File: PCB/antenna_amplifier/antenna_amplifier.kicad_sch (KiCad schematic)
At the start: 0 parts

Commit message: Populate antenna_amplifier schematic with full signal chain
Place all ICs (LMP7721, LMP7715, PCM1808, CS8406, 2x ADM7150),
passive components (R1/R3 220k filter, R2 1k + C3 4.7u feedback,
R4 470R guard drive), connectors (ANT_IN, SPDIF_OUT, PWR_IN),
and power symbols (+9V, +5VA, +3V3D, GND).

Wire signal path: antenna → RC filter → LMP7721 preamp with
frequency-dependent feedback → PCM1808 ADC (I2S) → CS8406
SPDIF TX → output connector. Guard driver (LMP7715 unity-gain)
drives PCB guard ring. Dual ADM7150 LDOs for analog/digital
supply rails.

All CS8406 config pins tied for HW mode, I2S input, 256fs.
Netlist verified correct (28 nets, 0 unconnected pins).
Remaining ERC: lib_symbol_mismatch (cosmetic), label placement,
PWR_FLAG needed on GND/+9V — all fixable in KiCad editor.

Co-Authored-By: Claude Opus 4.6 <noreply@anthropic.com>
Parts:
- added C3: 4.7u, symbol Device:C
- added J1: ANT_IN, symbol Connector:Conn_01x02_Pin
- added J2: SPDIF_OUT, symbol Connector:Conn_01x02_Pin
- added J3: PWR_IN, symbol Connector:Conn_01x02_Pin
- added R1, R3: 220k, symbol Device:R
- added R2: 1k, symbol Device:R
- added R4: 470, symbol Device:R
- added U1: LMP7721, Package_SO:SOIC-8_3.9x4.9mm_P1.27mm, symbol antenna_amplifier:LMP7721
- added U2: LMP7715, Package_TO_SOT_SMD:SOT-23-5, symbol antenna_amplifier:LMP7715
- added U3: PCM1808, Package_SO:TSSOP-14_4.4x5mm_P0.65mm, symbol antenna_amplifier:PCM1808
- added U4: CS8406, Package_SO:TSSOP-28_4.4x9.7mm_P0.65mm, symbol antenna_amplifier:CS8406
- added U5: ADM7150-5.0, Package_SO:SOIC-8-1EP_3.9x4.9mm_P1.27mm_EP2.41x3.1mm, symbol antenna_amplifier:ADM7150
- added U6: ADM7150-3.3, Package_SO:SOIC-8-1EP_3.9x4.9mm_P1.27mm_EP2.41x3.1mm, symbol antenna_amplifier:ADM7150
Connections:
- new net: R1.2, R3.1
- new net: R4.1, U2.1 (OUT), U2.4 (-IN)
- new net +3V3D: U3.4 (VDD), U4.16 (CEN), U4.23 (VL), U4.5 (SFMT1), U4.6 (VD), U4.9 (~{RST}), U6.2 (VOUT)
- new net +5VA: U1.8 (V+), U2.5 (V+), U3.3 (VCC), U5.2 (VOUT)
- new net +9V: J3.1 (Pin_1), U5.7 (EN), U5.8 (VIN), U6.7 (EN), U6.8 (VIN)
- new net ANT_IN: J1.1 (Pin_1), R1.1
- new net BCK: U3.8 (BCK), U4.13 (ISCLK)
- new net BIAS_MID: U3.1 (VREF), U3.14 (VINR)
- new net BYP_A: U5.3 (BYP)
- new net BYP_D: U6.3 (BYP)
- new net DOUT: U3.9 (DOUT), U4.14 (SDIN)
- new net FILT_OUT: R3.2, U1.1 (IN+), U2.3 (+IN)
- new net GND: J1.2 (Pin_2), J3.2 (Pin_2), U1.4 (V-), U2.2 (V-), U3.10 (MD0), U3.11 (MD1), U3.12 (FMT), U3.2 (AGND), U3.5 (DGND), U4.1 (COPY/C), U4.10 (APMS), U4.11 (TCBLD), U4.17 (V), U4.18 (U), U4.19 (AUDIO), U4.2 (TEST), U4.20 (HWCK0), U4.22 (GND), U4.24 (~{H/S}), U4.27 (HWCK1), U4.28 (ORIG), U4.3 (EMPH), U4.4 (SFMT0), U4.7 (TEST), U4.8 (TEST), U5.4 (GND), U5.9 (EPAD), U6.4 (GND), U6.9 (EPAD)
- new net GUARD_RING: R4.2, U1.2 (GRD), U1.7 (GRD)
- new net LRCK: U3.7 (LRCK), U4.12 (ILRCK)
- new net MCLK: U3.6 (SCKI), U4.21 (OMCK)
- new net PREAMP_OUT: C3.1, C3.2, R2.1, R2.2, U1.3 (IN-), U1.6 (VOUT), U3.13 (VINL)
- new net REFS_A: U5.5 (REF_SENSE)
- new net REFS_D: U6.5 (REF_SENSE)
- new net REF_A: U5.6 (REF)
- new net REF_D: U6.6 (REF)
- new net SPDIF_N: J2.2 (Pin_2), U4.25 (TXN)
- new net SPDIF_P: J2.1 (Pin_1), U4.26 (TXP)
- new net TCBL: U4.15 (TCBL)
- new net VREG_A: U5.1 (VREG)
- new net VREG_D: U6.1 (VREG)
- no-connect marks 0 -> 1
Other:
- title: (none) -> ELARA  ELF/VLF Atmospheric Radio Analyser

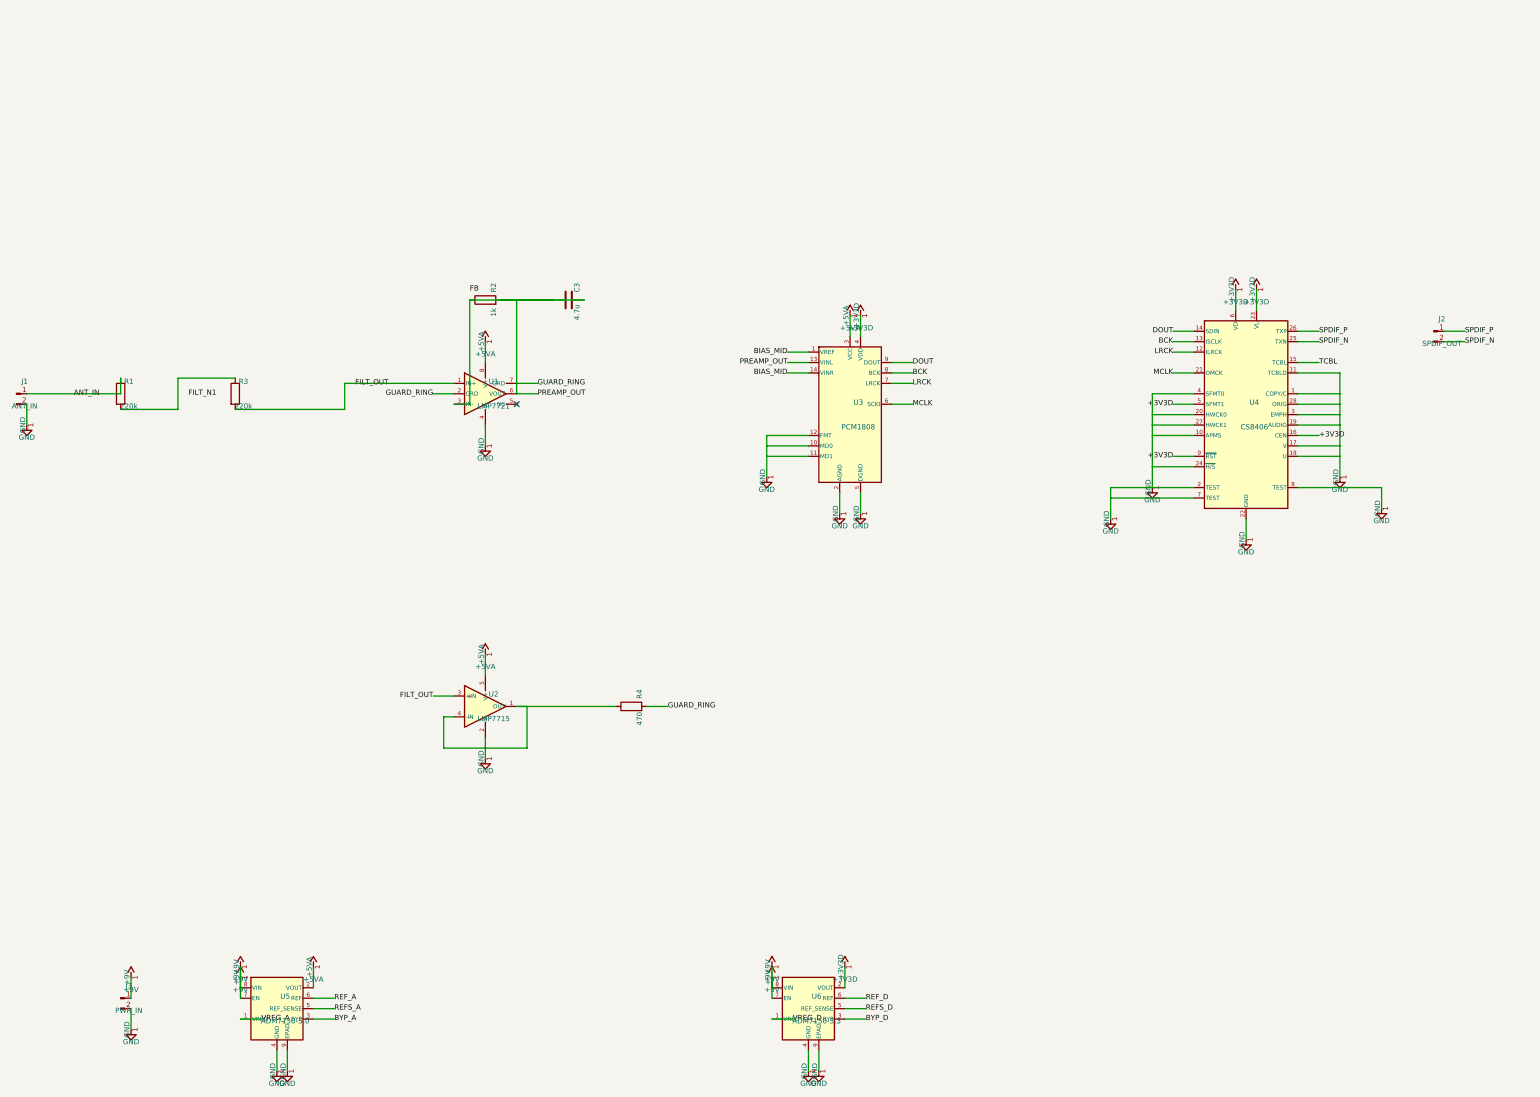
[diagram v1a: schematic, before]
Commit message: Fix preamp feedback, add bias/oscillator/AA filter (Phases 1-4)
Phase 1 — Fix feedback network for 20 dB ELF gain:
  R2→Rf (9.1k), C3→Cf (150nF) in parallel IN-→VOUT,
  add Rg (1k) from IN-→BIAS_MID. G=10.1 (20dB) flat across
  ELF, rolls off above 117 Hz. Correct single-supply biasing
  via 2.5V BIAS_MID reference.

Phase 2 — Add antenna bias circuit (§3.7):
  U7 LMP7715 unity-gain follower, R5/R6 47k matched divider
  (+5VA→GND → 2.5V), C7 4700µF bypass, C8 100nF supply bypass,
  J4 jumper header for physical antenna connection.
  BIAS_MID net shared with preamp Rg reference.

Phase 3 — Add 24.576 MHz MEMS oscillator:
  Y1 MEMS_OSC with R_S 33R series resistor, C9 100nF bypass.
  MCLK net drives PCM1808 SCKI and CS8406 OMCK.
  New MEMS_OSC symbol added to project library.

Phase 4 — Add anti-aliasing filter (§3.4):
  R_AA (10k) + C_AA (100nF) passive RC, fc=159 Hz.
  Inserted between PREAMP_OUT and AA_OUT→PCM1808 VINL.
  Combined with preamp rolloff (117 Hz) gives ~2nd-order
  filtering for ELF-focused design.

Co-Authored-By: Claude Opus 4.6 (1M context) <noreply@anthropic.com>
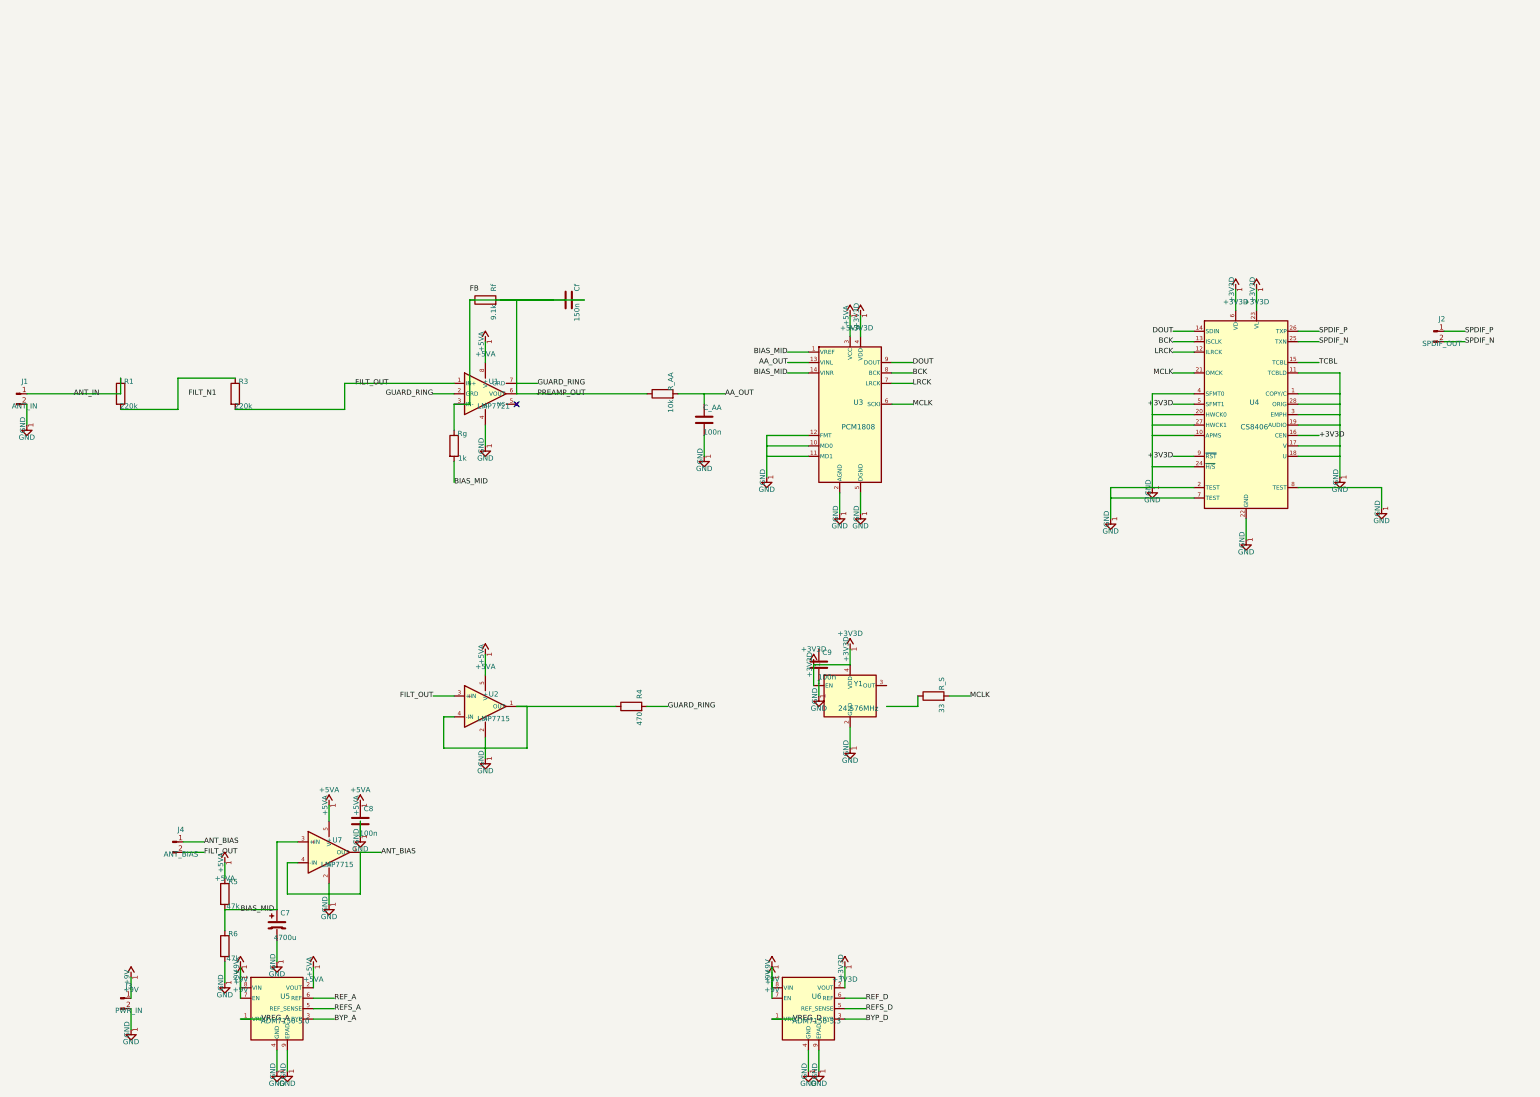
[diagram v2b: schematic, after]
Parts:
- added C7: 4700u, symbol Device:C_Polarized
- added C8, C9, C_AA: 100n, symbol Device:C
- added J4: ANT_BIAS, symbol Connector:Conn_01x02_Pin
- added R5, R6: 47k, symbol Device:R
- added R_AA: 10k, symbol Device:R
- added R_S: 33, symbol Device:R
- added Rg: 1k, symbol Device:R
- added U7: LMP7715, Package_TO_SOT_SMD:SOT-23-5, symbol antenna_amplifier:LMP7715
- added Y1: 24.576MHz, Package_TO_SOT_SMD:SOT-23-5, symbol antenna_amplifier:MEMS_OSC
- Cf: renamed from C3; value 4.7u -> 150n
- Rf: renamed from R2; value 1k -> 9.1k
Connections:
- net +3V3D: now also Y1.1 (EN), Y1.4 (VDD)
- net +5VA: now also C8.1, R5.1, U7.5 (V+)
- net BIAS_MID: now also C7.1, R5.2, R6.1, Rg.2, U7.3 (+IN)
- net FILT_OUT: now also J4.2 (Pin_2)
- net GND: now also C7.2, C8.2, C9.2, C_AA.2, R6.2, U7.2 (V-), Y1.2 (GND)
- net MCLK: now also R_S.2
- net PREAMP_OUT: now also R_AA.1, Rg.1; no longer U3.13 (VINL)
- new net AA_OUT: C_AA.1, R_AA.2, U3.13 (VINL)
- new net ANT_BIAS: J4.1 (Pin_1), U7.1 (OUT), U7.4 (-IN)
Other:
- title: ELARA  ELF/VLF Atmospheric Radio Analyser -> ELARA � ELF/VLF Atmospheric Radio Analyser

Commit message: Add transformers, fix config pins, update PLAN.md (Phases 5-8)
Phase 5 — Add audio transformers + dual output:
  TR1 (S22082) for S/PDIF coax → J2 RCA,
  TR2 (S22083) for AES/EBU balanced → J5 connector.
  Coupling caps C_T1/C_T2 (100nF) on primaries.
  Both driven from CS8406 TXP/TXN simultaneously.
  New XFMR_Audio symbol added to project library.

Phase 6 — Fix PCM1808 config for 96 kSPS default:
  MD1 changed from GND to +5VA (MD1=H, MD0=L → 256×fs).

Phase 8 — Update PLAN.md:
  - Revised §3.1: new feedback topology (Rf=9.1k, Cf=150nF,
    Rg=1k to BIAS_MID), 20 dB flat ELF gain, 117 Hz rolloff
  - Documented ELF-only design decision (VLF dropped)
  - Updated §3.4: simplified AA filter (R_AA 10k + C_AA 100nF,
    fc=159 Hz, combined with preamp rolloff for 2nd-order)
  - Title updated: ELF/VLF → ELF

Phase 7 (bypass caps) deferred to KiCad GUI placement.

Co-Authored-By: Claude Opus 4.6 (1M context) <noreply@anthropic.com>
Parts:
- added C_T1, C_T2: 100n, symbol Device:C
- added J5: AES_EBU, symbol Connector:Conn_01x02_Pin
- added TR1: S22082, symbol antenna_amplifier:XFMR_Audio
- added TR2: S22083, symbol antenna_amplifier:XFMR_Audio
- J2: value SPDIF_OUT -> SPDIF_COAX
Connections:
- net GND is gone; now on net +5VA: C7.2, C8.2, C9.2, C_AA.2, J1.2 (Pin_2), J3.2 (Pin_2), R6.2, U1.4 (V-), U2.2 (V-), U3.10 (MD0), U3.11 (MD1), U3.12 (FMT), U3.2 (AGND), U3.5 (DGND), U4.1 (COPY/C), U4.10 (APMS), U4.11 (TCBLD), U4.17 (V), U4.18 (U), U4.19 (AUDIO), U4.2 (TEST), U4.20 (HWCK0), U4.22 (GND), U4.24 (~{H/S}), U4.27 (HWCK1), U4.28 (ORIG), U4.3 (EMPH), U4.4 (SFMT0), U4.7 (TEST), U4.8 (TEST), U5.4 (GND), U5.9 (EPAD), U6.4 (GND), U6.9 (EPAD), U7.2 (V-), Y1.2 (GND)
- net +5VA: now also U4.26 (TXP), C_T1.1, C_T2.1
- net SPDIF_N: now also TR1.2 (P2), TR2.2 (P2); no longer J2.2 (Pin_2)
- net SPDIF_P: no longer names the net of J2.1 (Pin_1)
- net SPDIF_P: now also TR1.3 (S1); no longer U4.26 (TXP)
- new net: C_T1.2, TR1.1 (P1)
- new net: C_T2.2, TR2.1 (P1)
- new net: J5.1 (Pin_1), TR2.3 (S1)
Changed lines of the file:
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@@
 	)
+	(symbol
+		(lib_id "antenna_amplifier:XFMR_Audio")
+		(at 368.3 55.88 0)
+		(unit 1)
+		(exclude_from_sim no) (in_bom yes) (on_board yes) (dnp no)
+		(property "Reference" "TR1" (at 368.3 46.99 0) (effects (font (size 1.27 1.27))))
+		(property "Value" "S22082" (at 368.3 64.77 0) (effects (font (size 1.27 1.27))))
+		(property "Datasheet" "~" (at 368.3 55.88 0) (effects (font (size 1.27 1.27)) (hide yes)))
+		(instances (project "antenna_amplifier"
+			(path "/09f45598-3e76-49a4-ba12-a3a92a2874f1" (reference "TR1") (unit 1)))))
+	(symbol
+		(lib_id "antenna_amplifier:XFMR_Audio")
+		(at 368.3 78.74 0)
+		(unit 1)
+		(exclude_from_sim no) (in_bom yes) (on_board yes) (dnp no)
+		(property "Reference" "TR2" (at 368.3 69.85 0) (effects (font (size 1.27 1.27))))
+		(property "Value" "S22083" (at 368.3 87.63 0) (effects (font (size 1.27 1.27))))
+		(property "Datasheet" "~" (at 368.3 78.74 0) (effects (font (size 1.27 1.27)) (hide yes)))
+		(instances (project "antenna_amplifier"
+			(path "/09f45598-3e76-49a4-ba12-a3a92a2874f1" (reference "TR2") (unit 1)))))
 	(symbol
 		(lib_id "Connector:Conn_01x02_Pin")
-		(at 370.84 63.5 0)
-		(unit 1)
-		(exclude_from_sim no)
-		(in_bom yes)
-		(on_board yes)
-		(dnp no)
-		(property "Reference" "J2"
-			(at 372.84 60.5 0)
-			(effects
-				(font
-					(size 1.27 1.27)
-				)
-			)
-		)
-		(property "Value" "SPDIF_OUT"
-			(at 372.84 66.5 0)
-			(effects
-				(font
-					(size 1.27 1.27)
-				)
-			)
-		)
-		(property "Datasheet" "~"
-			(at 370.84 63.5 0)
-			(effects
-				(font
-					(size 1.27 1.27)
-				)
-				(hide yes)
-			)
-		)
-		(instances
-			(project "antenna_amplifier"
-				(path "/09f45598-3e76-49a4-ba12-a3a92a2874f1"
-					(reference "J2")
-					(unit 1)
-				)
-			)
-		)
-	)
+		(at 386.08 55.88 0)
+		(unit 1)
+		(exclude_from_sim no) (in_bom yes) (on_board yes) (dnp no)
+		(property "Reference" "J2" (at 388.08 52.88 0) (effects (font (size 1.27 1.27))))
+		(property "Value" "SPDIF_COAX" (at 388.08 58.88 0) (effects (font (size 1.27 1.27))))
+		(property "Datasheet" "~" (at 386.08 55.88 0) (effects (font (size 1.27 1.27)) (hide yes)))
+		(instances (project "antenna_amplifier"
+			(path "/09f45598-3e76-49a4-ba12-a3a92a2874f1" (reference "J2") (unit 1)))))
+	(symbol
+		(lib_id "Connector:Conn_01x02_Pin")
+		(at 386.08 78.74 0)
+		(unit 1)
+		(exclude_from_sim no) (in_bom yes) (on_board yes) (dnp no)
+		(property "Reference" "J5" (at 388.08 75.74 0) (effects (font (size 1.27 1.27))))
+		(property "Value" "AES_EBU" (at 388.08 81.74 0) (effects (font (size 1.27 1.27))))
+		(property "Datasheet" "~" (at 386.08 78.74 0) (effects (font (size 1.27 1.27)) (hide yes)))
+		(instances (project "antenna_amplifier"
+			(path "/09f45598-3e76-49a4-ba12-a3a92a2874f1" (reference "J5") (unit 1)))))
+	(symbol
+		(lib_id "Device:C")
+		(at 355.6 50.8 90)
+		(unit 1)
+		(exclude_from_sim no) (in_bom yes) (on_board yes) (dnp no)
+		(property "Reference" "C_T1" (at 355.6 47.8 0) (effects (font (size 1.27 1.27))))
+		(property "Value" "100n" (at 355.6 53.8 0) (effects (font (size 1.27 1.27))))
+		(property "Datasheet" "~" (at 355.6 50.8 0) (effects (font (size 1.27 1.27)) (hide yes)))
+		(instances (project "antenna_amplifier"
+			(path "/09f45598-3e76-49a4-ba12-a3a92a2874f1" (reference "C_T1") (unit 1)))))
+	(symbol
+		(lib_id "Device:C")
+		(at 355.6 73.66 90)
+		(unit 1)
+		(exclude_from_sim no) (in_bom yes) (on_board yes) (dnp no)
+		(property "Reference" "C_T2" (at 355.6 70.66 0) (effects (font (size 1.27 1.27))))
+		(property "Value" "100n" (at 355.6 76.66 0) (effects (font (size 1.27 1.27))))
+		(property "Datasheet" "~" (at 355.6 73.66 0) (effects (font (size 1.27 1.27)) (hide yes)))
+		(instances (project "antenna_amplifier"
+			(path "/09f45598-3e76-49a4-ba12-a3a92a2874f1" (reference "C_T2") (unit 1)))))
+	(wire (pts (xy 351.79 50.8) (xy 347.98 50.8))
+		(stroke (width 0) (type solid)))
+	(label "SPDIF_P" (at 347.98 50.8 180)
+		(effects (font (size 1.27 1.27))))
+	(wire (pts (xy 359.41 50.8) (xy 363.22 50.8))
+		(stroke (width 0) (type solid)))
+	(wire (pts (xy 363.22 60.96) (xy 358.14 60.96))
+		(stroke (width 0) (type solid)))
+	(label "SPDIF_N" (at 358.14 60.96 180)
+		(effects (font (size 1.27 1.27))))
+	(wire (pts (xy 373.38 50.8) (xy 378.46 50.8))
+		(stroke (width 0) (type solid)))
+	(wire (pts (xy 378.46 50.8) (xy 378.46 55.88))
+		(stroke (width 0) (type solid)))
+	(wire (pts (xy 378.46 55.88) (xy 388.62 55.88))
+		(stroke (width 0) (type solid)))
+	(wire (pts (xy 373.38 60.96) (xy 381 60.96))
+		(stroke (width 0) (type solid)))
+	(wire (pts (xy 381 60.96) (xy 381 53.34))
+		(stroke (width 0) (type solid)))
+	(wire (pts (xy 381 53.34) (xy 388.62 53.34))
+		(stroke (width 0) (type solid)))
+	(wire (pts (xy 351.79 73.66) (xy 347.98 73.66))
+		(stroke (width 0) (type solid)))
+	(label "SPDIF_P" (at 347.98 73.66 180)
+		(effects (font (size 1.27 1.27))))
+	(wire (pts (xy 359.41 73.66) (xy 363.22 73.66))
+		(stroke (width 0) (type solid)))
+	(wire (pts (xy 363.22 83.82) (xy 358.14 83.82))
+		(stroke (width 0) (type solid)))
+	(label "SPDIF_N" (at 358.14 83.82 180)
+		(effects (font (size 1.27 1.27))))
+	(wire (pts (xy 373.38 73.66) (xy 378.46 73.66))
+		(stroke (width 0) (type solid)))
+	(wire (pts (xy 378.46 73.66) (xy 378.46 78.74))
+		(stroke (width 0) (type solid)))
+	(wire (pts (xy 378.46 78.74) (xy 388.62 78.74))
+		(stroke (width 0) (type solid)))
+	(wire (pts (xy 373.38 83.82) (xy 381 83.82))
+		(stroke (width 0) (type solid)))
+	(wire (pts (xy 381 83.82) (xy 381 76.2))
+		(stroke (width 0) (type solid)))
+	(wire (pts (xy 381 76.2) (xy 388.62 76.2))
+		(stroke (width 0) (type solid)))
 	(symbol
 		(lib_id "Connector:Conn_01x02_Pin")
@@
 	(wire
 		(pts
-			(xy 218.44 93.98) (xy 208.28 93.98)
-		)
-		(stroke
-			(width 0)
-			(type solid)
-		)
-	)
+			(xy 218.44 93.98) (xy 218.44 88.9)
+		)
+		(stroke
+			(width 0)
+			(type solid)
+		)
+	)
+	(symbol
+		(lib_id "power:+5VA")
+		(at 218.44 88.9 0)
+		(unit 1)
+		(exclude_from_sim no) (in_bom yes) (on_board yes) (dnp no)
+		(property "Reference" "#PWR80" (at 218.44 86.9 0) (effects (font (size 1.27 1.27)) (hide yes)))
+		(property "Value" "+5VA" (at 218.44 85.09 0) (effects (font (size 1.27 1.27))))
+		(instances (project "antenna_amplifier"
+			(path "/09f45598-3e76-49a4-ba12-a3a92a2874f1" (reference "#PWR80") (unit 1)))))
 	(wire
 		(pts
@@
 	(wire
 		(pts
-			(xy 208.28 91.44) (xy 208.28 93.98)
-		)
-		(stroke
-			(width 0)
-			(type solid)
-		)
-	)
-	(wire
-		(pts
-			(xy 208.28 93.98) (xy 208.28 99.06)
+			(xy 208.28 91.44) (xy 208.28 99.06)
 		)
 		(stroke
@@
 		(effects
 			(font
-				(size 1.27 1.27)
-			)
-		)
-	)
-	(wire
-		(pts
-			(xy 373.38 63.5) (xy 378.46 63.5)
-		)
-		(stroke
-			(width 0)
-			(type solid)
-		)
-	)
-	(label "SPDIF_P"
-		(at 378.46 63.5 0)
-		(effects
-			(font
-				(size 1.27 1.27)
-			)
-		)
-	)
-	(wire
-		(pts
-			(xy 373.38 66.04) (xy 378.46 66.04)
-		)
-		(stroke
-			(width 0)
-			(type solid)
-		)
-	)
-	(label "SPDIF_N"
-		(at 378.46 66.04 0)
-		(effects
-			(font
